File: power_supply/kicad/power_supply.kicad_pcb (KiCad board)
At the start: 2 copper layers, 90 x 88.4 mm, 19 parts, among them J1 pcie_98, J2 Conn_01x05_Socket, U1 URB2405YMD-10WR3, U2 ESD5344D

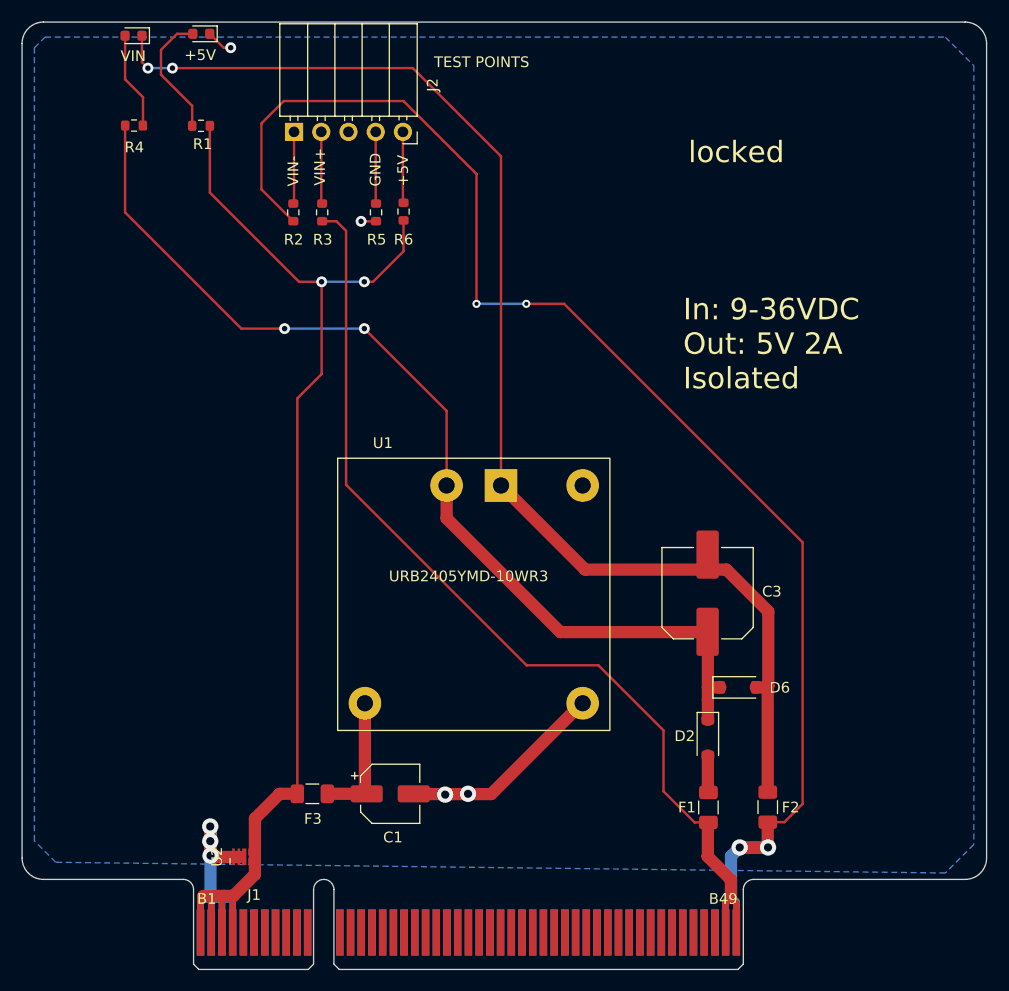
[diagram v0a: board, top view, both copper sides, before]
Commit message: Final touches of the power supply board, before ordering.
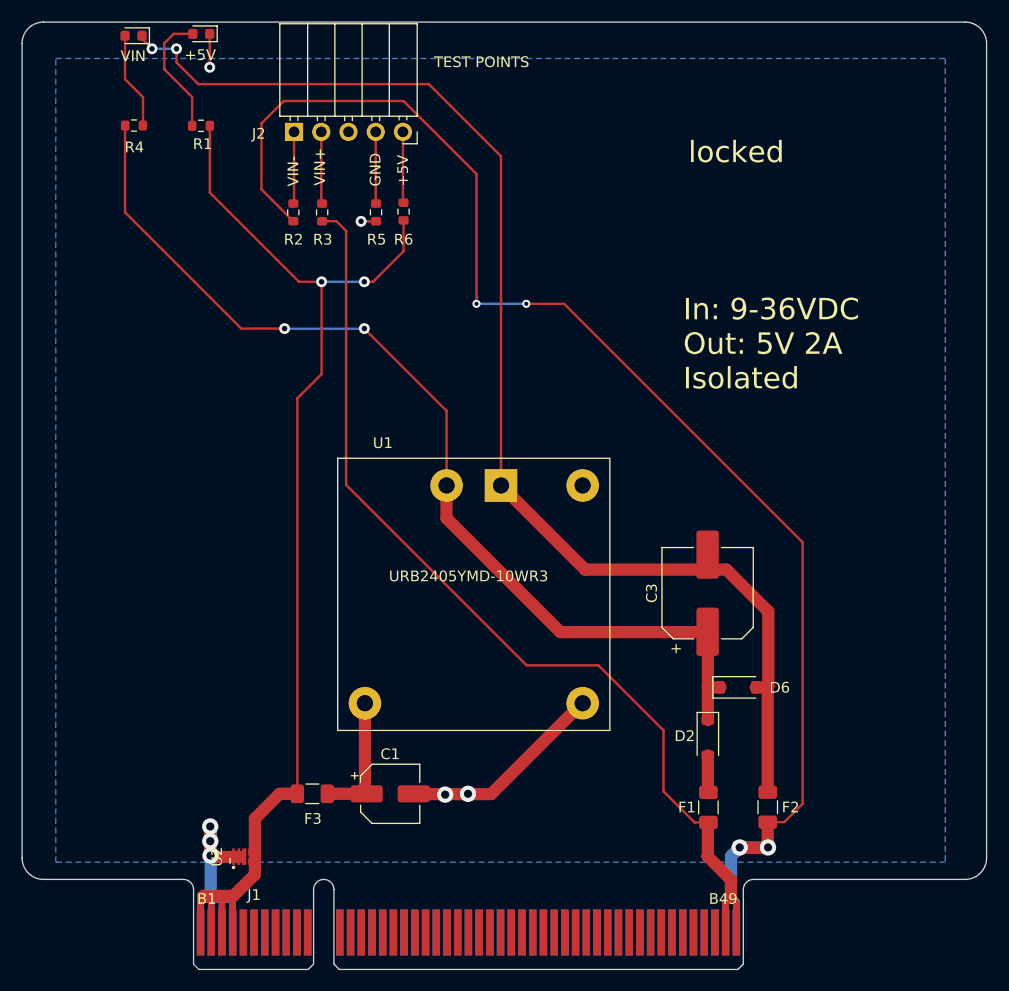
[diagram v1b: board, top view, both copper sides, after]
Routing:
- net GND: track 52.6 -> 53.2 mm
- net Net-(D1-K): track 118.2 -> 117.7 mm
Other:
- board text added: "+"
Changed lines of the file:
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@@
     (fp_line (start -0.14 -1.32) (end -0.64 -1.32)
       (stroke (width 0.12) (type solid)) (layer "F.SilkS"))
+    (fp_circle (center -1 -1) (end -0.9 -1)
+      (stroke (width 0.12) (type solid)) (fill solid) (layer "F.SilkS"))
     (fp_line (start -0.95 -1.5) (end 0.95 -1.5)
       (stroke (width 0.05) (type solid)) (layer "F.CrtYd"))
@@
     (property "ki_keywords" "connector")
     (attr through_hole)
-    (fp_text reference "J2" (at 7.85 -4.38 -90) (layer "F.SilkS")
+    (fp_text reference "J2" (at -8.3766 0.172) (layer "F.SilkS")
         (effects (font (size 1 1) (thickness 0.15)))
     )
@@
     (property "ki_keywords" "cap capacitor")
     (attr smd)
-    (fp_text reference "C3" (at 0.1524 5.9944 180) (layer "F.SilkS")
+    (fp_text reference "C3" (at 0 -5.2 90) (layer "F.SilkS")
         (effects (font (size 1 1) (thickness 0.15)))
     )
@@
     (property "ki_keywords" "cap capacitor")
     (attr smd)
-    (fp_text reference "C1" (at 0.254 4.064) (layer "F.SilkS")
+    (fp_text reference "C1" (at 0 -3.7) (layer "F.SilkS")
         (effects (font (size 1 1) (thickness 0.15)))
     )
@@
     (effects (font (size 2 2) (thickness 0.2)) (justify left bottom))
   )
+  (gr_text "+" (at 102.3112 30.6324) (layer "F.SilkS")
+    (effects (font (size 1 1) (thickness 0.15)) (justify left bottom))
+  )
   (gr_text "TEST POINTS" (at 80.2894 -24.6634) (layer "F.SilkS")
     (effects (font (size 1 1) (thickness 0.15)) (justify left))
@@
     (effects (font (size 1 1) (thickness 0.15)) (justify left))
   )
-  (segment (start 78.4254 43.6372) (end 78.4 43.6118) (width 1.143) (layer "F.Cu") (net 1))
+  (segment (start 59.3599 -27.305) (end 59.3598 -24.1808) (width 0.2286) (layer "F.Cu") (net 1))
   (segment (start 59.436 49.0982) (end 59.4106 49.0728) (width 1.143) (layer "F.Cu") (net 1))
   (segment (start 85.6234 43.6372) (end 78.4254 43.6372) (width 1.143) (layer "F.Cu") (net 1))
@@
   (segment (start 94.16 35.16) (end 94.1006 35.16) (width 1.143) (layer "F.Cu") (net 1))
   (segment (start 94.1006 35.16) (end 85.6234 43.6372) (width 1.143) (layer "F.Cu") (net 1))
-  (segment (start 59.3599 -27.305) (end 60.6553 -26.0096) (width 0.2286) (layer "F.Cu") (net 1))
-  (segment (start 60.6553 -26.0096) (end 61.3156 -26.0096) (width 0.2286) (layer "F.Cu") (net 1))
   (segment (start 74.866 -9.8044) (end 73.4822 -9.8044) (width 0.2286) (layer "F.Cu") (net 1))
   (segment (start 62.1792 49.5046) (end 59.563 49.5046) (width 1.143) (layer "F.Cu") (net 1))
-  (via (at 61.3156 -26.0096) (size 1.016) (drill 0.508) (layers "F.Cu" "B.Cu") (net 1))
+  (via (at 59.3598 -24.1808) (size 1.016) (drill 0.508) (layers "F.Cu" "B.Cu") (net 1))
   (via (at 83.4644 43.6118) (size 1.524) (drill 0.762) (layers "F.Cu" "B.Cu") (net 1))
   (via (at 59.4106 48.0314) (size 1.524) (drill 0.762) (layers "F.Cu" "B.Cu") (net 1))
@@
   (segment (start 53.1226 -18.7452) (end 53.1368 -18.7594) (width 0.2286) (layer "F.Cu") (net 92))
   (segment (start 53.1368 -21.3868) (end 51.4603 -23.0633) (width 0.2286) (layer "F.Cu") (net 92))
-  (segment (start 56.3118 -27.305) (end 54.8132 -25.8064) (width 0.2286) (layer "F.Cu") (net 93))
-  (segment (start 57.7849 -27.305) (end 56.3118 -27.305) (width 0.2286) (layer "F.Cu") (net 93))
-  (segment (start 54.8132 -25.8064) (end 54.8132 -23.495) (width 0.2286) (layer "F.Cu") (net 93))
-  (segment (start 54.8132 -23.495) (end 57.722 -20.5862) (width 0.2286) (layer "F.Cu") (net 93))
-  (segment (start 57.722 -20.5862) (end 57.722 -18.7198) (width 0.2286) (layer "F.Cu") (net 93))
+  (segment (start 56.007 -27.305) (end 55.118 -26.416) (width 0.2286) (layer "F.Cu") (net 93))
+  (segment (start 57.7849 -27.305) (end 56.007 -27.305) (width 0.2286) (layer "F.Cu") (net 93))
+  (segment (start 57.722 -21.399) (end 57.722 -18.7198) (width 0.2286) (layer "F.Cu") (net 93))
+  (segment (start 55.118 -26.416) (end 55.118 -24.003) (width 0.2286) (layer "F.Cu") (net 93))
+  (segment (start 55.118 -24.003) (end 57.722 -21.399) (width 0.2286) (layer "F.Cu") (net 93))
   (segment (start 67.2284 -11.5384) (end 67.1576 -11.4676) (width 0.2286) (layer "F.Cu") (net 95))
   (segment (start 67.2284 -18.1552) (end 67.2284 -11.5384) (width 0.2286) (layer "F.Cu") (net 95))
@@
   (via (at 73.787002 0.2032) (size 1.016) (drill 0.508) (layers "F.Cu" "B.Cu") (net 101))
   (segment (start 66.3448 0.2032) (end 73.787002 0.2032) (width 0.2286) (layer "B.Cu") (net 101))
-  (segment (start 55.88 -24.1046) (end 78.3082 -24.1046) (width 0.2286) (layer "F.Cu") (net 102))
+  (segment (start 53.0353 -27.1272) (end 53.0353 -26.8477) (width 0.2286) (layer "F.Cu") (net 102))
   (segment (start 111.3536 33.6804) (end 111.4806 33.5534) (width 1.143) (layer "F.Cu") (net 102))
   (segment (start 111.4298 33.6042) (end 111.4806 33.5534) (width 1.143) (layer "F.Cu") (net 102))
+  (segment (start 79.8068 -22.606) (end 58.293 -22.606) (width 0.2286) (layer "F.Cu") (net 102))
   (segment (start 110.3112 33.6804) (end 111.3536 33.6804) (width 1.143) (layer "F.Cu") (net 102))
-  (segment (start 53.0353 -27.1272) (end 53.0353 -24.6633) (width 0.2286) (layer "F.Cu") (net 102))
   (segment (start 111.4298 43.4564) (end 111.4298 33.6042) (width 1.143) (layer "F.Cu") (net 102))
   (segment (start 94.392 22.692) (end 86.54 14.84) (width 1.143) (layer "F.Cu") (net 102))
-  (segment (start 86.54 -15.8728) (end 86.54 14.84) (width 0.2286) (layer "F.Cu") (net 102))
+  (segment (start 86.54 14.84) (end 86.54 -15.8728) (width 0.2286) (layer "F.Cu") (net 102))
+  (segment (start 53.0353 -26.8477) (end 53.975 -25.908) (width 0.2286) (layer "F.Cu") (net 102))
+  (segment (start 58.293 -22.606) (end 56.261 -24.638) (width 0.2286) (layer "F.Cu") (net 102))
   (segment (start 111.4806 33.5534) (end 111.4806 26.5938) (width 1.143) (layer "F.Cu") (net 102))
   (segment (start 111.4806 26.5938) (end 107.5788 22.692) (width 1.143) (layer "F.Cu") (net 102))
-  (segment (start 53.0353 -24.6633) (end 53.594 -24.1046) (width 0.2286) (layer "F.Cu") (net 102))
-  (segment (start 78.3082 -24.1046) (end 86.54 -15.8728) (width 0.2286) (layer "F.Cu") (net 102))
+  (segment (start 86.54 -15.8728) (end 79.8068 -22.606) (width 0.2286) (layer "F.Cu") (net 102))
+  (segment (start 56.261 -24.638) (end 56.261 -25.908) (width 0.2286) (layer "F.Cu") (net 102))
   (segment (start 107.5788 22.692) (end 94.392 22.692) (width 1.143) (layer "F.Cu") (net 102))
-  (via (at 55.88 -24.1046) (size 1.016) (drill 0.508) (layers "F.Cu" "B.Cu") (net 102))
-  (via (at 53.594 -24.1046) (size 1.016) (drill 0.508) (layers "F.Cu" "B.Cu") (net 102))
-  (segment (start 53.594 -24.1046) (end 55.88 -24.1046) (width 0.2286) (layer "B.Cu") (net 102))
+  (via (at 56.261 -25.908) (size 1.016) (drill 0.508) (layers "F.Cu" "B.Cu") (net 102))
+  (via (at 53.975 -25.908) (size 1.016) (drill 0.508) (layers "F.Cu" "B.Cu") (net 102))
+  (segment (start 53.975 -25.908) (end 56.261 -25.908) (width 0.2286) (layer "B.Cu") (net 102))
   (zone (net 1) (net_name "GND") (layer "B.Cu") (hatch edge 0.508)
-    (connect_pads (clearance 0.381))
+    (connect_pads (clearance 1))
     (min_thickness 0.254) (filled_areas_thickness no)
-    (fill yes (thermal_gap 0.508) (thermal_bridge_width 0.762))
+    (fill yes (thermal_gap 0.508) (thermal_bridge_width 0.762) (smoothing fillet) (radius 4))
     (polygon
       (pts
-        (xy 43 48)
-        (xy 43 -26)
-        (xy 44 -27)
-        (xy 128 -27)
-        (xy 130.6604 -24.3396)
-        (xy 130.6604 48.3396)
-        (xy 128 51)
+        (xy 45 -25)
+        (xy 128 -25)
+        (xy 128 50)
         (xy 45 50)
       )

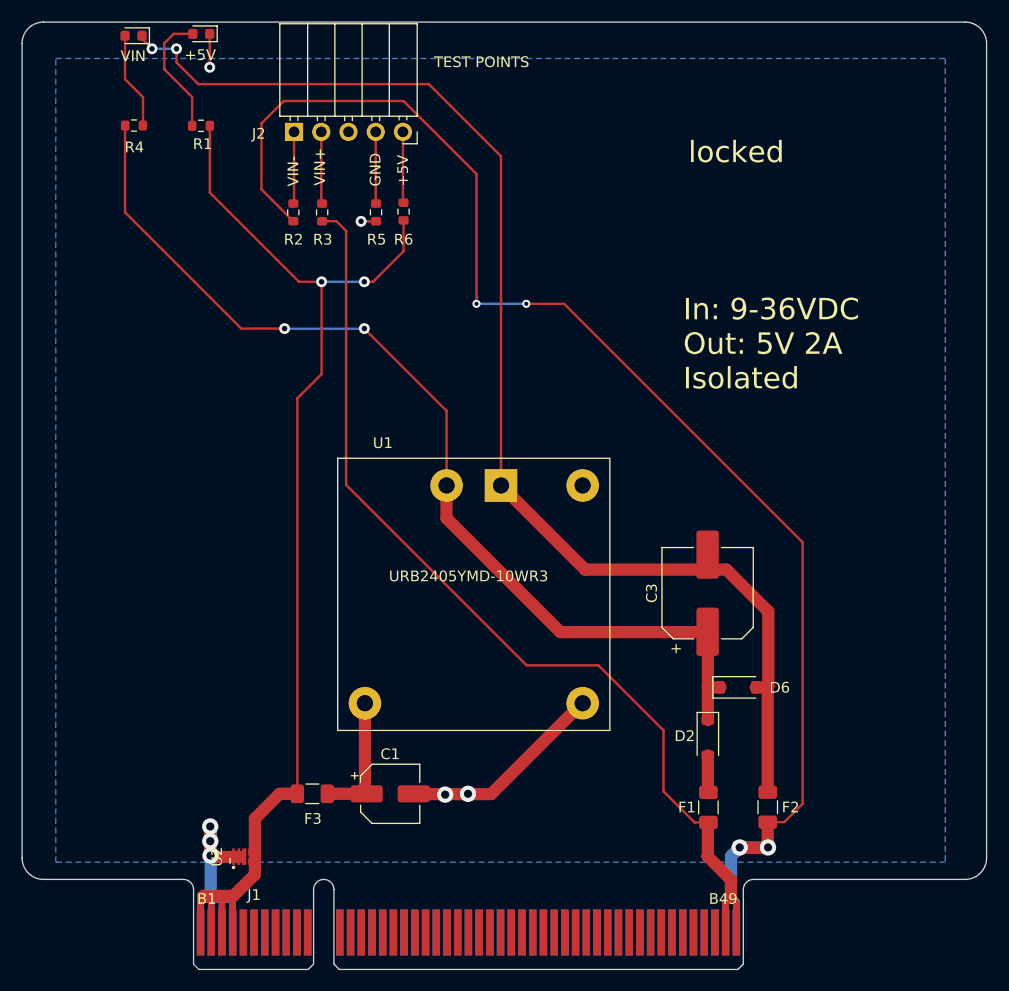
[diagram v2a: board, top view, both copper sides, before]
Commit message: Cleaned up TODOs of the power supply board.
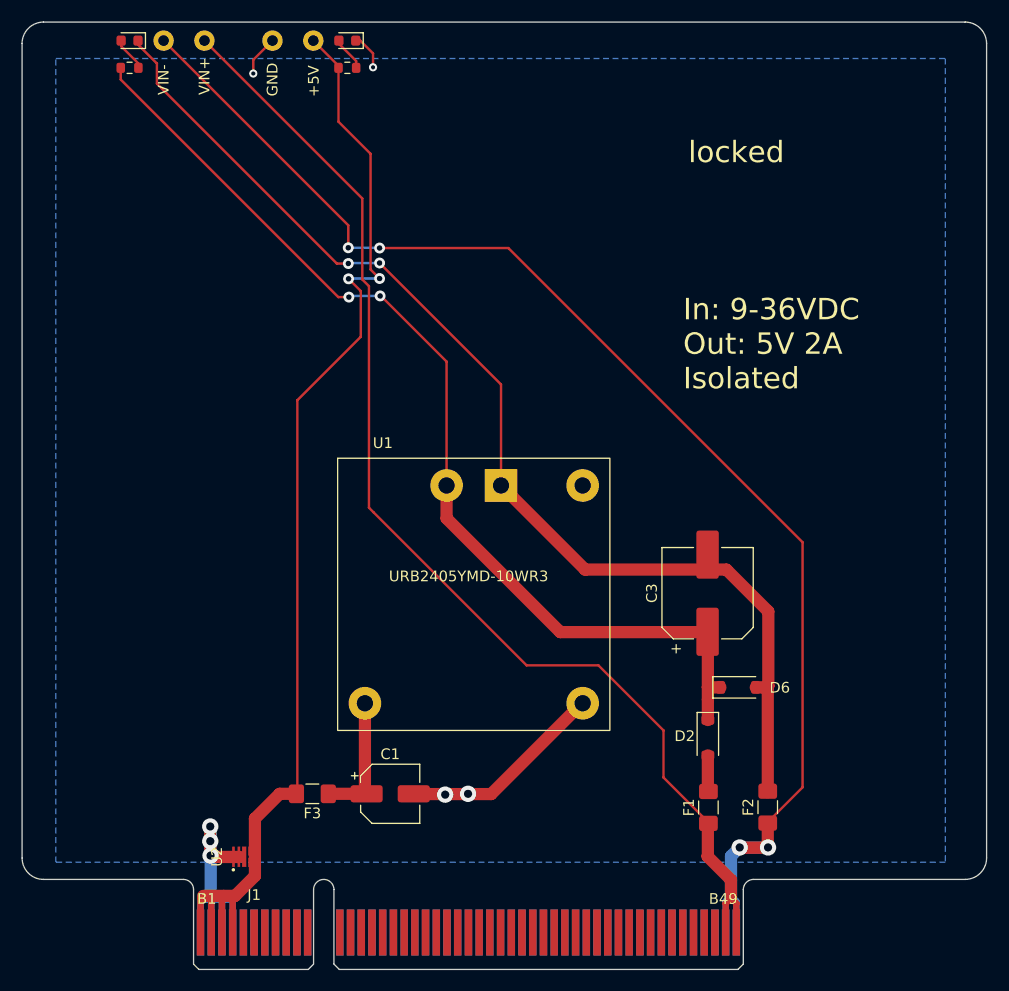
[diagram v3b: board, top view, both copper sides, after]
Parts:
- removed J2: Conn_01x05_Socket, common:PinSocket_1x05_P2.54mm_Horizontal_JLCPCB
- removed R2, R3, R5, R6: 1K, Resistor_SMD:R_0603_1608Metric
- added TP1: TestPoint, common:Test_Pad, F.Cu at (55.1, -26.7)
- added TP2: TestPoint, common:Test_Pad, F.Cu at (58.9, -26.7)
- added TP3: TestPoint, common:Test_Pad, F.Cu at (65.2, -26.7)
- added TP4: TestPoint, common:Test_Pad, F.Cu at (69.0, -26.7)
- F1, F2, F3: footprint Fuse:Fuse_1206_3216Metric -> Fuse:Fuse_1206_3216Metric_Pad1.42x1.75mm_HandSolder
- R1: value 3K9 -> 6K8
- moved R1 14.7 mm to (72.2, -24.1), turned to 0 degrees
- moved D5 13.6 mm to (72.2, -26.7)
- moved R4 5.40 mm to (51.9, -24.1)
- moved D1 0.59 mm to (51.9, -26.7)
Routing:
- net /VIN+: track 91.3 -> 111.2 mm
- net Net-(D1-K): track 117.7 -> 105.9 mm
- net Net-(D5-A): track 11.8 -> 3.21 mm
- net Net-(J2-Pin_2): track 6.72 -> 0.00 mm
- net Net-(J2-Pin_1): track 6.72 -> 0.00 mm
- net Net-(J2-Pin_4): track 6.70 -> 0.00 mm
- net Net-(J2-Pin_5): track 6.63 -> 0.00 mm
- net /VIN-: track 134.0 -> 127.5 mm
- net Net-(D1-A): track 9.08 -> 3.21 mm
- net GND: track 53.2 -> 55.9 mm
- net /+5V: track 110.2 -> 108.4 mm
- net Net-(D2-K): track 94.0 -> 95.3 mm
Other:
- board text removed: "TEST POINTS"
- board text removed: "VIN"

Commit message: Minor tweak of the schematics.
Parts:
- F1, F2, F3: footprint Fuse:Fuse_1206_3216Metric_Pad1.42x1.75mm_HandSolder -> common:Fuse_1206_3216Metric_Pad1.42x1.75mm_HandSolder
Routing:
- net GND: track 55.9 -> 41.7 mm
